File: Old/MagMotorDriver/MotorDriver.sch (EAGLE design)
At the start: 17 parts

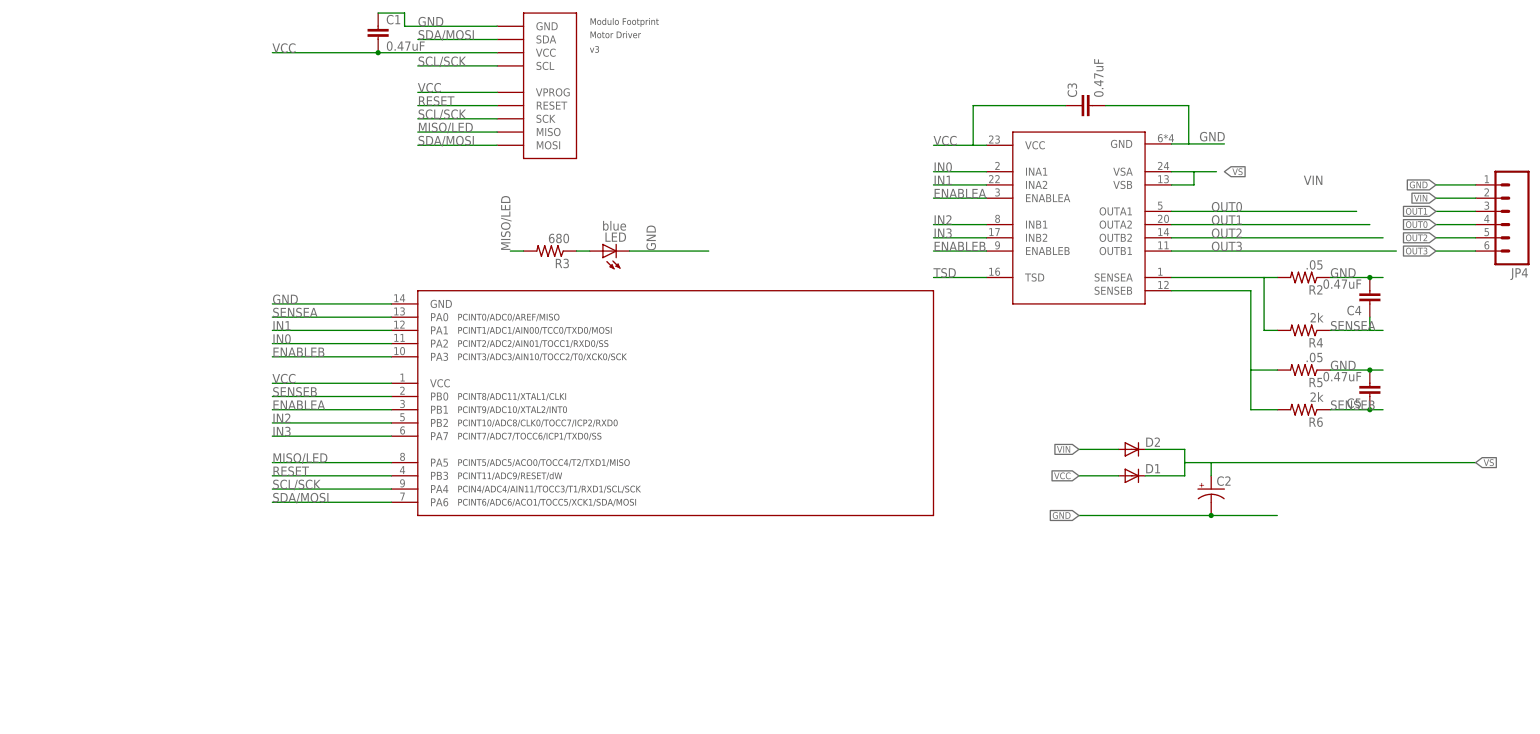
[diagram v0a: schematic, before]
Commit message: Moved a bunch of files around
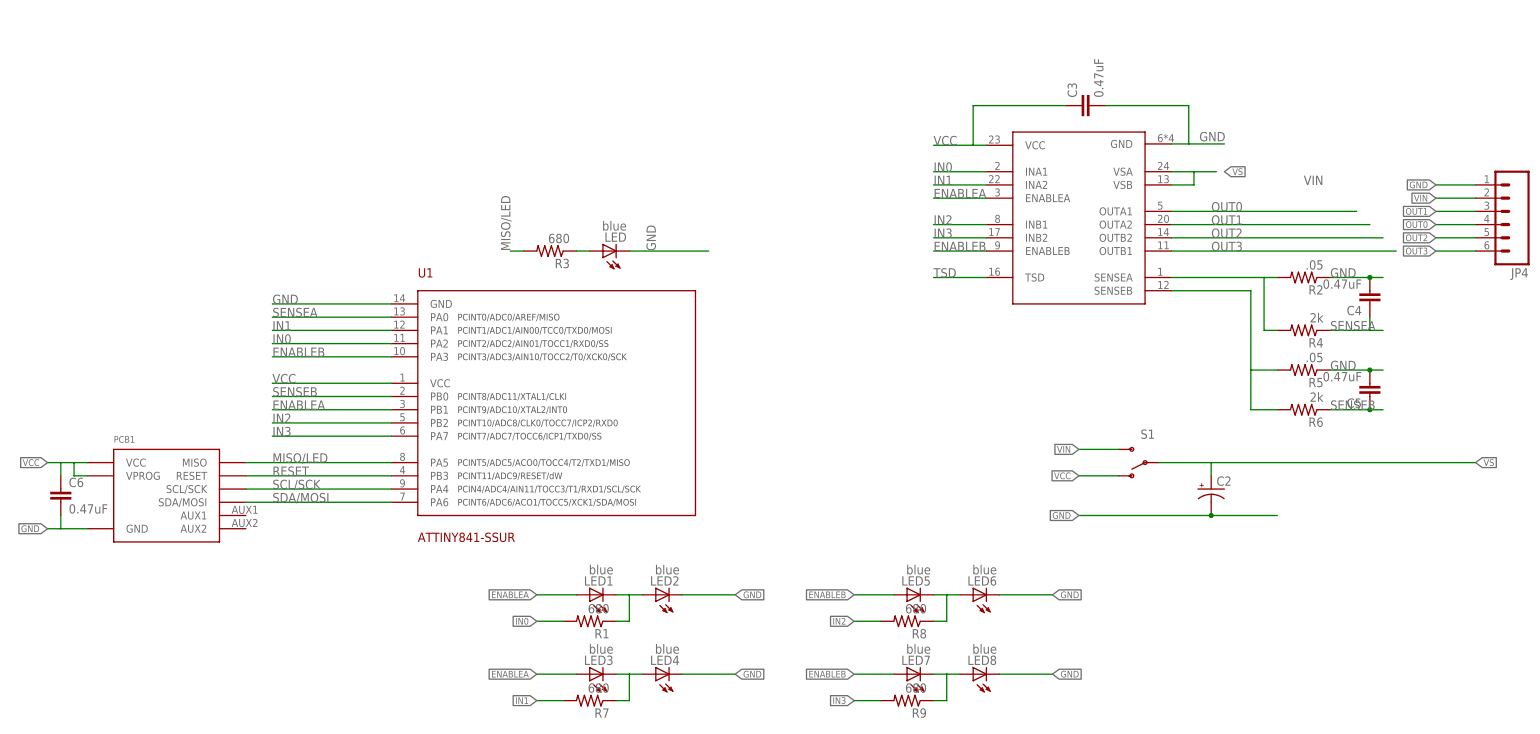
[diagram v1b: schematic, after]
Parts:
- removed C1: 0.47uF, SparkFun-Capacitors:CAP0805
- removed D1, D2: (no value), SparkFun-DiscreteSemi:DIODESMA
- removed U$1: FOOTPRINTFOOTPRINT-2, IntegerLabs:FOOTPRINTFOOTPRINT-2
- removed U$3: TINY841, IntegerLabs:TINY841
- added C6: 0.47uF, SparkFun-Capacitors:CAP0805
- added LED1, LED2, LED3, LED4, LED5, LED6, LED7, LED8: blue, Modulo:LED-0805-BLUE
- added PCB1: MAGDEVICE-V2-DOUBLE, Modulo:MAGDEVICE-V2-DOUBLE
- added R1, R7, R8, R9: 680, SparkFun-Passives:RESISTOR0805-RES
- added S1: (no value), SparkFun-Electromechanical:SWITCH-SPDTPTH_LOCK
- added U1: ATTINY841-SSUR, Modulo:ATTINY841
- LED: device adafruit:LEDCHIPLED_0805 -> Modulo:LED-0805-BLUE
- renumbered U$6 to U2
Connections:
- new net N$1: LED1.C, LED2.A, R1.1
- new net N$4: LED3.C, LED4.A, R7.1
- new net N$6: LED5.C, LED6.A, R8.1
- new net N$7: LED7.C, LED8.A, R9.1
- net ENABLEA: now also LED1.A, LED3.A, U1.PB1; no longer U$3.PB1
- net ENABLEB: now also LED5.A, LED7.A, U1.PA3; no longer U$3.PA3
- net GND: now also C6.2, LED2.C, LED4.C, LED6.C, LED8.C, PCB1.GND, U1.GND; no longer C1.1, U$1.GND, U$3.GND
- net IN0: now also R1.2, U1.PA2; no longer U$3.PA2
- net IN1: now also R7.2, U1.PA1; no longer U$3.PA1
- net IN2: now also R8.2, U1.PB2; no longer U$3.PB2
- net IN3: now also R9.2, U1.PA7; no longer U$3.PA7
- net MISO/LED: now also PCB1.MISO, U1.PA5; no longer U$1.MISO, U$3.PA5
- net RESET: now also PCB1.RESET, U1.PB3; no longer U$1.RESET, U$3.PB3
- net SCL/SCK: now also PCB1.SCL/SCK, U1.PA4; no longer U$1.SCK, U$1.SCL, U$3.PA4
- net SDA/MOSI: now also PCB1.SDA/MOSI, U1.PA6; no longer U$1.MOSI, U$1.SDA, U$3.PA6
- net SENSEA: now also U1.PA0; no longer U$3.PA0
- net SENSEB: now also U1.PB0; no longer U$3.PB0
- net VCC: now also C6.1, PCB1.VCC, PCB1.VPROG, S1.O, U1.VCC; no longer C1.2, D1.A, U$1.VCC, U$1.VPROG, U$3.VCC
- net VIN: now also S1.S; no longer D2.A
- net VS: now also S1.P; no longer D1.C, D2.C
